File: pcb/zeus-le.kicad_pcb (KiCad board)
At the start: 6 copper layers, 50 x 50 mm, 81 parts, among them J1 12402012E212A, J2 S2B-PH-SM4-TB, J3 B5B-PH-K-S, J4 BD125-10-A-0305-0580-L-B, J5 MSD-1-A, J6 B2B-PH-K-S, SW1 EVQPUD02K, U1 NUF2042XV6T1G, U10 D3V3F4U6S-7, U2 RT6160AWSC, U3 KTS1662EUW-TR, U4 BQ25150YFPR, U5 TLV320ADC6120IRTER, U6 WT02C40C-V3, U7 AP21510FM-7, U8 TPD6F003DQDR, U9 LP5810ADSDR

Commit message: pcb: rev 1.0 version submitted for manufacturing
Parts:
- moved SW1 0.10 mm to (171.1, 105.3)
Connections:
- U5 pad 12: /Audio/I2C.SCL -> /Audio/I2C.SDA
- U5 pad 13: /Audio/I2C.SDA -> /Audio/I2C.SCL
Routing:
- net /Audio/I2C.SDA: track 125.5 -> 128.1 mm
- net /Audio/I2C.SCL: track 119.6 -> 117.7 mm
- net GND: vias 115 -> 116

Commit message: pcb: remove stray trace
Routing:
- net GND: track 57.6 -> 56.7 mm

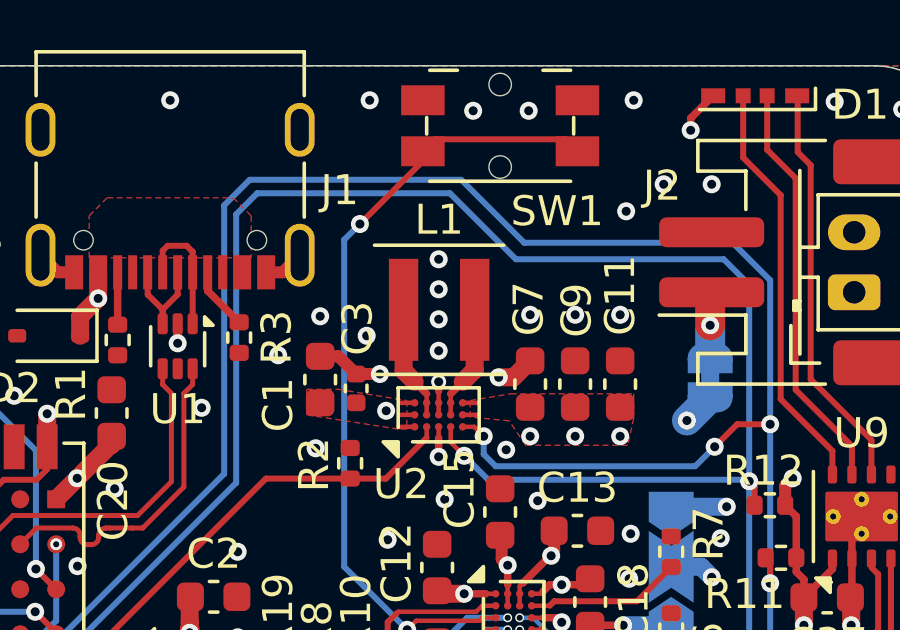
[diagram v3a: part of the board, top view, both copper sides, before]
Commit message: pcb: replace inductor
Replace power supply inductor with a more readily available and cheaper
part.
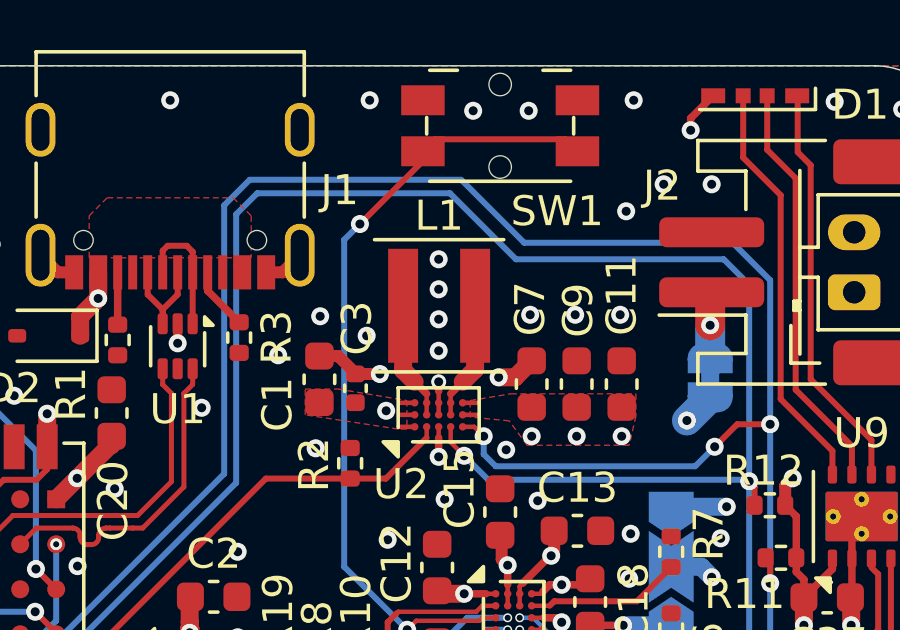
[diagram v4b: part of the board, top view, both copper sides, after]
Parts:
- L1: footprint Inductor_SMD:L_Coilcraft_XxL4020 -> zeus-le:L_Bourns_SRP4020FA_4.1x4.1mm
- moved L1 0.14 mm to (169.1, 111.3)
- moved C11 0.05 mm to (175.2, 113.9)
- moved C7 0.05 mm to (172.2, 113.9)
- moved C9 0.05 mm to (173.7, 113.9)

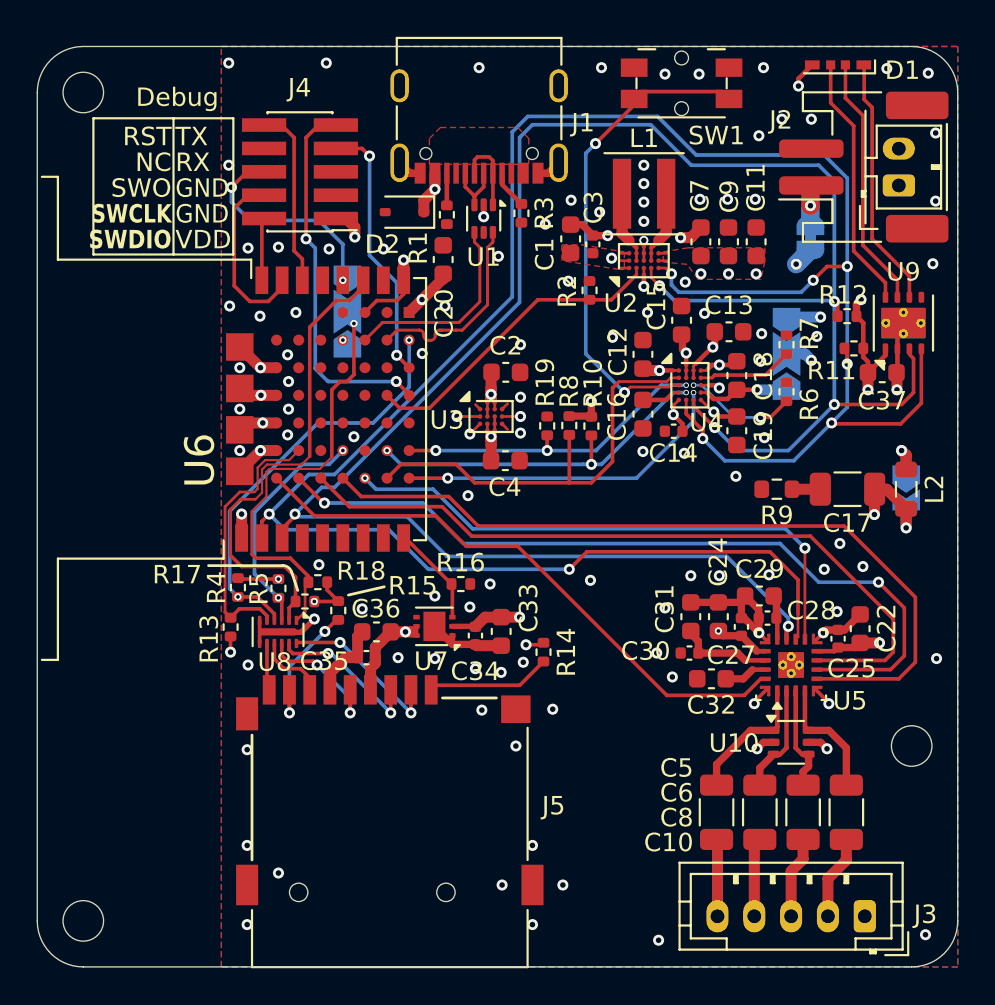
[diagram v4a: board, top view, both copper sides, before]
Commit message: pcb: add pull-downs for WiFi power
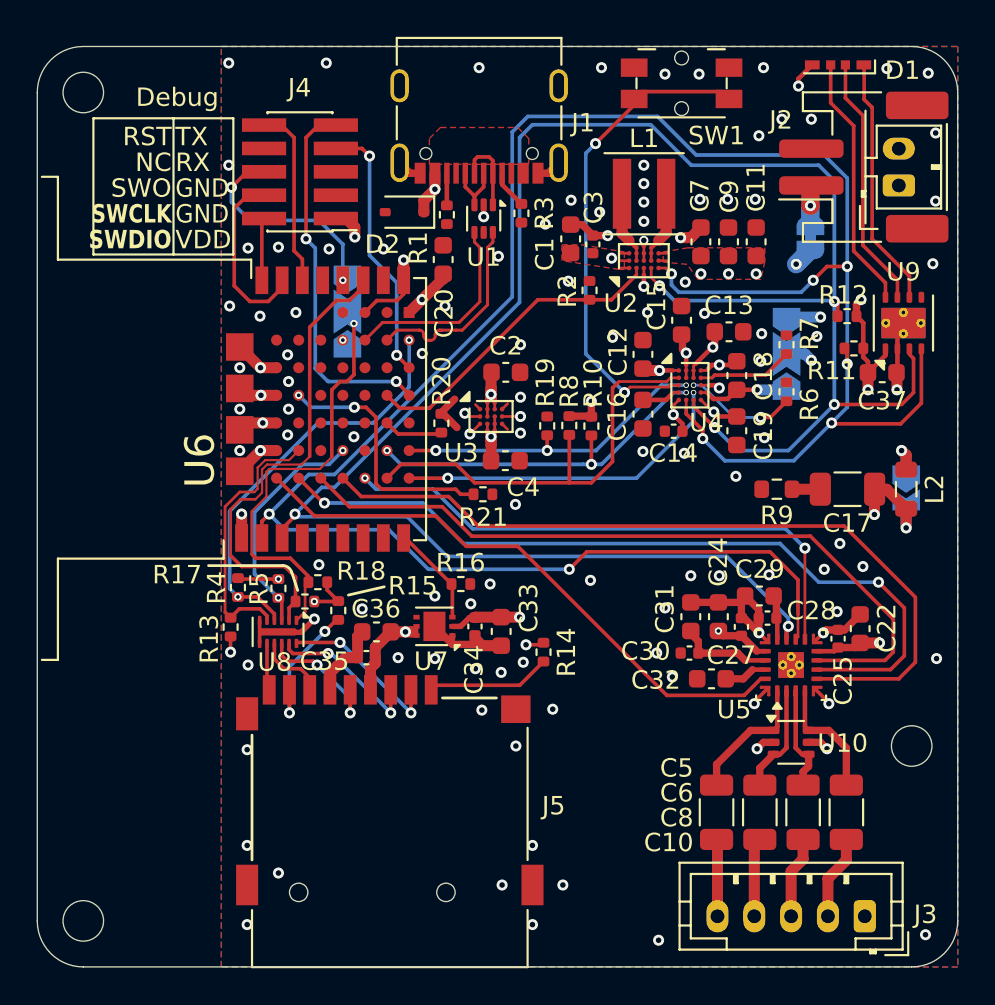
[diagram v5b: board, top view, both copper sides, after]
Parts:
- added R20: 100k, Resistor_SMD:R_0402_1005Metric, F.Cu at (158.1, 123.8)
- added R21: 100k, Resistor_SMD:R_0402_1005Metric, F.Cu at (160.3, 127.6)
- U3: value KTS1662EUW-TR -> KTS1662EUW-TR
- moved C34 0.50 mm to (159.9, 134.8)
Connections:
- U6 pad B5: unconnected-(U6-P012-PadB5) -> Net-(U6-P012)
- U6 pad C1: unconnected-(U6-P031-PadC1) -> Net-(U6-P031)
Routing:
- net Net-(U6-P031): track 0.00 -> 13.8 mm, vias 0 -> 2
- net Net-(U6-P012): track 0.00 -> 3.15 mm
- net GND: track 56.8 -> 59.6 mm

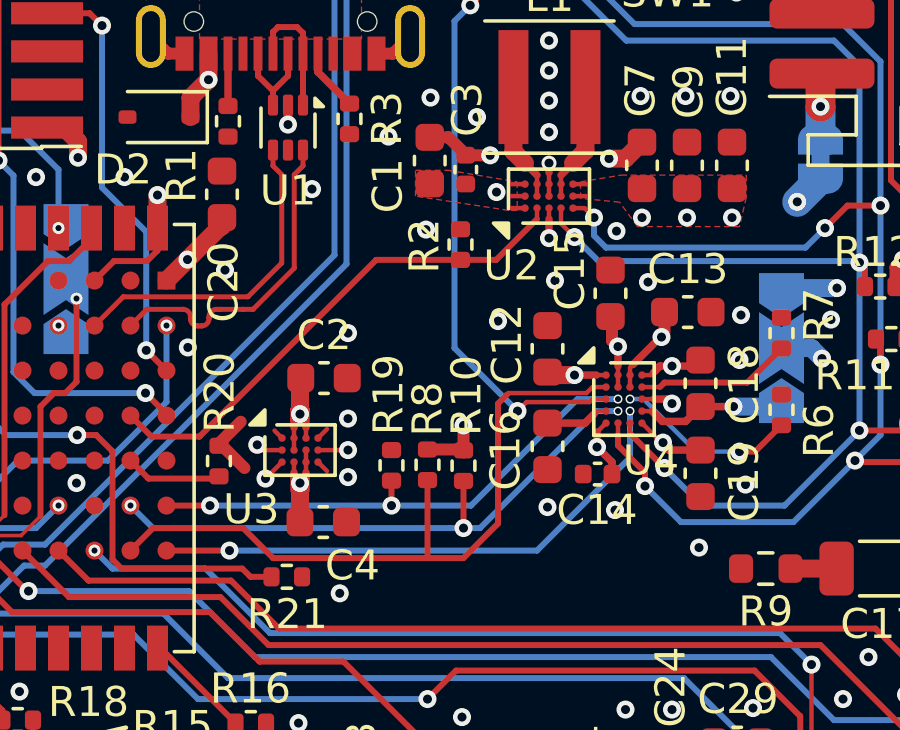
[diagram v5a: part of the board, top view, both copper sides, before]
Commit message: pcb: apply changes from manufacturing
* Increase WLCSP stencil clearance to -10%
* Use SMD WLCSP pads, dimensions from JLCPCB gerbers
* Copper margin around NPTH, only those in my library so far
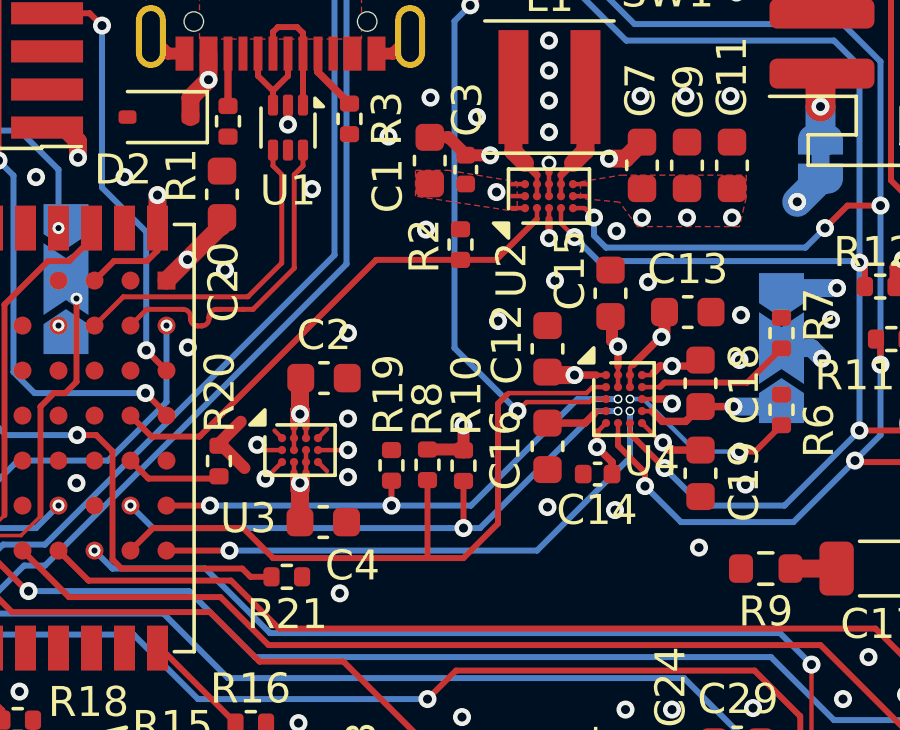
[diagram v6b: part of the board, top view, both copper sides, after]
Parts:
- U2: footprint zeus-le:Richtek_WLCSP-15_1.4x2.3mm_Layout3x5_P0.4mm_NSMD -> zeus-le:Richtek_WLCSP-15_1.4x2.3mm_Layout3x5_P0.4mm_SMD
- U3: footprint zeus-le:Kinetic_WLCSP-12_1.94x1.28mm_Layout4x3_P0.4mm_Ball0.25mm_Pad0.25mm_NSMD -> zeus-le:Kinetic_WLCSP-12_1.94x1.28mm_Layout4x3_P0.4mm_Ball0.25mm_Pad0.25mm_SMD
- U4: footprint zeus-le:Texas_DSBGA-20_1.615x2.015mm_Layout4x5_P0.4mm_NSMD -> zeus-le:Texas_DSBGA-20_1.615x2.015mm_Layout4x5_P0.4mm_SMD
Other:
- board text added: "rev 1.1"
- board text removed: "rev 1.0"
